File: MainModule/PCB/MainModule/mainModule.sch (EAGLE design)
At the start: 13 parts, among them U1 LM5007MM

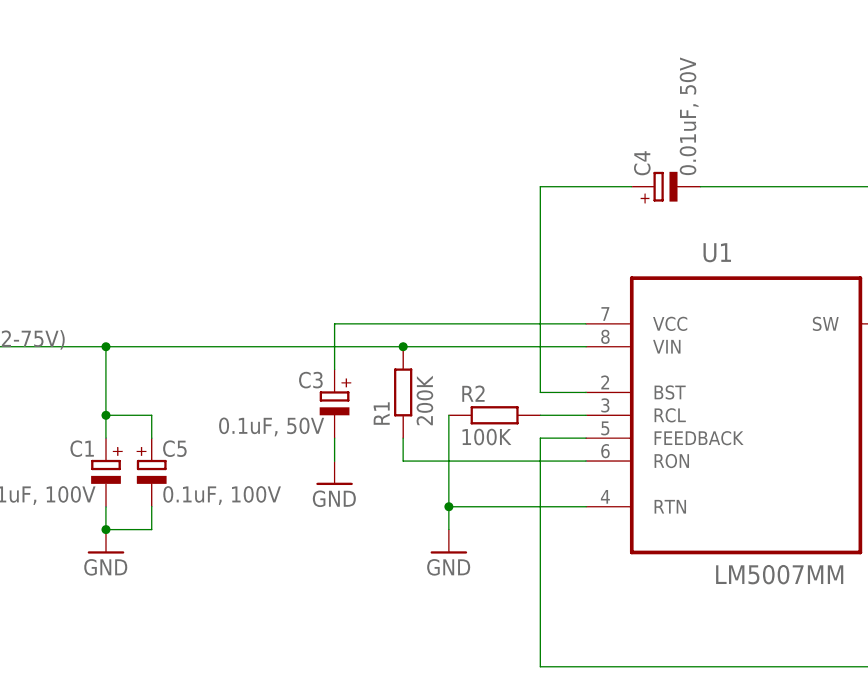
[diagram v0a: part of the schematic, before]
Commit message: Changed capacitor packages in to power supply schematic (switching)
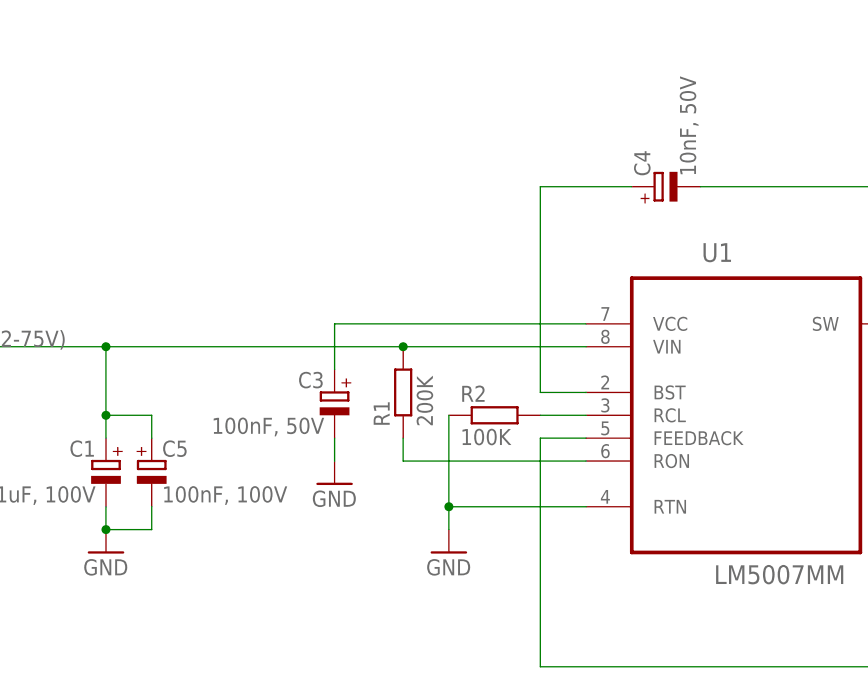
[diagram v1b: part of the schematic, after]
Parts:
- C1: device resistor:CPOL-EU140CLH-0810 -> resistor:CPOL-EU153CLV-0405
- C2: device resistor:CPOL-EU140CLH-0810 -> resistor:CPOL-EUC
- C3: value 0.1uF, 50V -> 100nF, 50V; device resistor:CPOL-EU140CLH-0810 -> resistor:CPOL-EUSMCA
- C4: value 0.01uF, 50V -> 10nF, 50V; device resistor:CPOL-EU140CLH-0810 -> resistor:CPOL-EUR/2012-12W
- C5: value 0.1uF, 100V -> 100nF, 100V; device resistor:CPOL-EU140CLH-0810 -> resistor:CPOL-EUSMCA
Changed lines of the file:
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@@
 <grid distance="0.1" unitdist="inch" unit="inch" style="lines" multiple="1" display="no" altdistance="0.01" altunitdist="inch" altunit="inch"/>
 <layers>
-<layer number="1" name="Top" color="4" fill="1" visible="no" active="no"/>
-<layer number="2" name="Route2" color="1" fill="3" visible="no" active="no"/>
-<layer number="3" name="Route3" color="4" fill="3" visible="no" active="no"/>
-<layer number="4" name="Route4" color="1" fill="4" visible="no" active="no"/>
-<layer number="5" name="Route5" color="4" fill="4" visible="no" active="no"/>
-<layer number="6" name="Route6" color="1" fill="8" visible="no" active="no"/>
-<layer number="7" name="Route7" color="4" fill="8" visible="no" active="no"/>
-<layer number="8" name="Route8" color="1" fill="2" visible="no" active="no"/>
-<layer number="9" name="Route9" color="4" fill="2" visible="no" active="no"/>
-<layer number="10" name="Route10" color="1" fill="7" visible="no" active="no"/>
-<layer number="11" name="Route11" color="4" fill="7" visible="no" active="no"/>
-<layer number="12" name="Route12" color="1" fill="5" visible="no" active="no"/>
-<layer number="13" name="Route13" color="4" fill="5" visible="no" active="no"/>
-<layer number="14" name="Route14" color="1" fill="6" visible="no" active="no"/>
-<layer number="15" name="Route15" color="4" fill="6" visible="no" active="no"/>
-<layer number="16" name="Bottom" color="1" fill="1" visible="no" active="no"/>
-<layer number="17" name="Pads" color="2" fill="1" visible="no" active="no"/>
-<layer number="18" name="Vias" color="2" fill="1" visible="no" active="no"/>
-<layer number="19" name="Unrouted" color="6" fill="1" visible="no" active="no"/>
-<layer number="20" name="Dimension" color="15" fill="1" visible="no" active="no"/>
-<layer number="21" name="tPlace" color="7" fill="1" visible="no" active="no"/>
-<layer number="22" name="bPlace" color="7" fill="1" visible="no" active="no"/>
-<layer number="23" name="tOrigins" color="15" fill="1" visible="no" active="no"/>
-<layer number="24" name="bOrigins" color="15" fill="1" visible="no" active="no"/>
-<layer number="25" name="tNames" color="7" fill="1" visible="no" active="no"/>
-<layer number="26" name="bNames" color="7" fill="1" visible="no" active="no"/>
-<layer number="27" name="tValues" color="7" fill="1" visible="no" active="no"/>
-<layer number="28" name="bValues" color="7" fill="1" visible="no" active="no"/>
+<layer number="1" name="Top" color="4" fill="1" visible="yes" active="no"/>
+<layer number="2" name="Route2" color="1" fill="3" visible="yes" active="no"/>
+<layer number="3" name="Route3" color="4" fill="3" visible="yes" active="no"/>
+<layer number="4" name="Route4" color="1" fill="4" visible="yes" active="no"/>
+<layer number="5" name="Route5" color="4" fill="4" visible="yes" active="no"/>
+<layer number="6" name="Route6" color="1" fill="8" visible="yes" active="no"/>
+<layer number="7" name="Route7" color="4" fill="8" visible="yes" active="no"/>
+<layer number="8" name="Route8" color="1" fill="2" visible="yes" active="no"/>
+<layer number="9" name="Route9" color="4" fill="2" visible="yes" active="no"/>
+<layer number="10" name="Route10" color="1" fill="7" visible="yes" active="no"/>
+<layer number="11" name="Route11" color="4" fill="7" visible="yes" active="no"/>
+<layer number="12" name="Route12" color="1" fill="5" visible="yes" active="no"/>
+<layer number="13" name="Route13" color="4" fill="5" visible="yes" active="no"/>
+<layer number="14" name="Route14" color="1" fill="6" visible="yes" active="no"/>
+<layer number="15" name="Route15" color="4" fill="6" visible="yes" active="no"/>
+<layer number="16" name="Bottom" color="1" fill="1" visible="yes" active="no"/>
+<layer number="17" name="Pads" color="2" fill="1" visible="yes" active="no"/>
+<layer number="18" name="Vias" color="2" fill="1" visible="yes" active="no"/>
+<layer number="19" name="Unrouted" color="6" fill="1" visible="yes" active="no"/>
+<layer number="20" name="Dimension" color="15" fill="1" visible="yes" active="no"/>
+<layer number="21" name="tPlace" color="7" fill="1" visible="yes" active="no"/>
+<layer number="22" name="bPlace" color="7" fill="1" visible="yes" active="no"/>
+<layer number="23" name="tOrigins" color="15" fill="1" visible="yes" active="no"/>
+<layer number="24" name="bOrigins" color="15" fill="1" visible="yes" active="no"/>
+<layer number="25" name="tNames" color="7" fill="1" visible="yes" active="no"/>
+<layer number="26" name="bNames" color="7" fill="1" visible="yes" active="no"/>
+<layer number="27" name="tValues" color="7" fill="1" visible="yes" active="no"/>
+<layer number="28" name="bValues" color="7" fill="1" visible="yes" active="no"/>
 <layer number="29" name="tStop" color="7" fill="3" visible="no" active="no"/>
 <layer number="30" name="bStop" color="7" fill="6" visible="no" active="no"/>
@@
 <layer number="35" name="tGlue" color="7" fill="4" visible="no" active="no"/>
 <layer number="36" name="bGlue" color="7" fill="5" visible="no" active="no"/>
-<layer number="37" name="tTest" color="7" fill="1" visible="no" active="no"/>
-<layer number="38" name="bTest" color="7" fill="1" visible="no" active="no"/>
+<layer number="37" name="tTest" color="7" fill="1" visible="yes" active="no"/>
+<layer number="38" name="bTest" color="7" fill="1" visible="yes" active="no"/>
 <layer number="39" name="tKeepout" color="4" fill="11" visible="no" active="no"/>
 <layer number="40" name="bKeepout" color="1" fill="11" visible="no" active="no"/>
@@
 <layer number="44" name="Drills" color="7" fill="1" visible="no" active="no"/>
 <layer number="45" name="Holes" color="7" fill="1" visible="no" active="no"/>
-<layer number="46" name="Milling" color="3" fill="1" visible="no" active="no"/>
-<layer number="47" name="Measures" color="7" fill="1" visible="no" active="no"/>
-<layer number="48" name="Document" color="7" fill="1" visible="no" active="no"/>
-<layer number="49" name="Reference" color="7" fill="1" visible="no" active="no"/>
-<layer number="51" name="tDocu" color="7" fill="1" visible="no" active="no"/>
-<layer number="52" name="bDocu" color="7" fill="1" visible="no" active="no"/>
+<layer number="46" name="Milling" color="3" fill="1" visible="yes" active="no"/>
+<layer number="47" name="Measures" color="7" fill="1" visible="yes" active="no"/>
+<layer number="48" name="Document" color="7" fill="1" visible="yes" active="no"/>
+<layer number="49" name="Reference" color="7" fill="1" visible="yes" active="no"/>
+<layer number="51" name="tDocu" color="7" fill="1" visible="yes" active="no"/>
+<layer number="52" name="bDocu" color="7" fill="1" visible="yes" active="no"/>
 <layer number="91" name="Nets" color="2" fill="1" visible="yes" active="yes"/>
 <layer number="92" name="Busses" color="1" fill="1" visible="yes" active="yes"/>
@@
 <part name="U1" library="LM5007" deviceset="LM5007MM" device=""/>
 <part name="FRAME1" library="frames" deviceset="A4L-LOC" device=""/>
-<part name="C1" library="resistor" deviceset="CPOL-EU" device="140CLH-0810" value="1uF, 100V"/>
-<part name="C2" library="resistor" deviceset="CPOL-EU" device="140CLH-0810" value="15uF, 25V"/>
-<part name="C3" library="resistor" deviceset="CPOL-EU" device="140CLH-0810" value="0.1uF, 50V"/>
-<part name="C4" library="resistor" deviceset="CPOL-EU" device="140CLH-0810" value="0.01uF, 50V"/>
-<part name="C5" library="resistor" deviceset="CPOL-EU" device="140CLH-0810" value="0.1uF, 100V"/>
+<part name="C1" library="resistor" deviceset="CPOL-EU" device="153CLV-0405" value="1uF, 100V"/>
+<part name="C2" library="resistor" deviceset="CPOL-EU" device="C" value="15uF, 25V"/>
+<part name="C3" library="resistor" deviceset="CPOL-EU" device="SMCA" value="100nF, 50V"/>
+<part name="C4" library="resistor" deviceset="CPOL-EU" device="R/2012-12W" value="10nF, 50V"/>
+<part name="C5" library="resistor" deviceset="CPOL-EU" device="SMCA" value="100nF, 100V"/>
 <part name="L1" library="inductor-neosid" deviceset="SM-Z15" device="" value="100uH"/>
 <part name="R1" library="rcl" deviceset="R-EU_" device="R2010" value="200K"/>

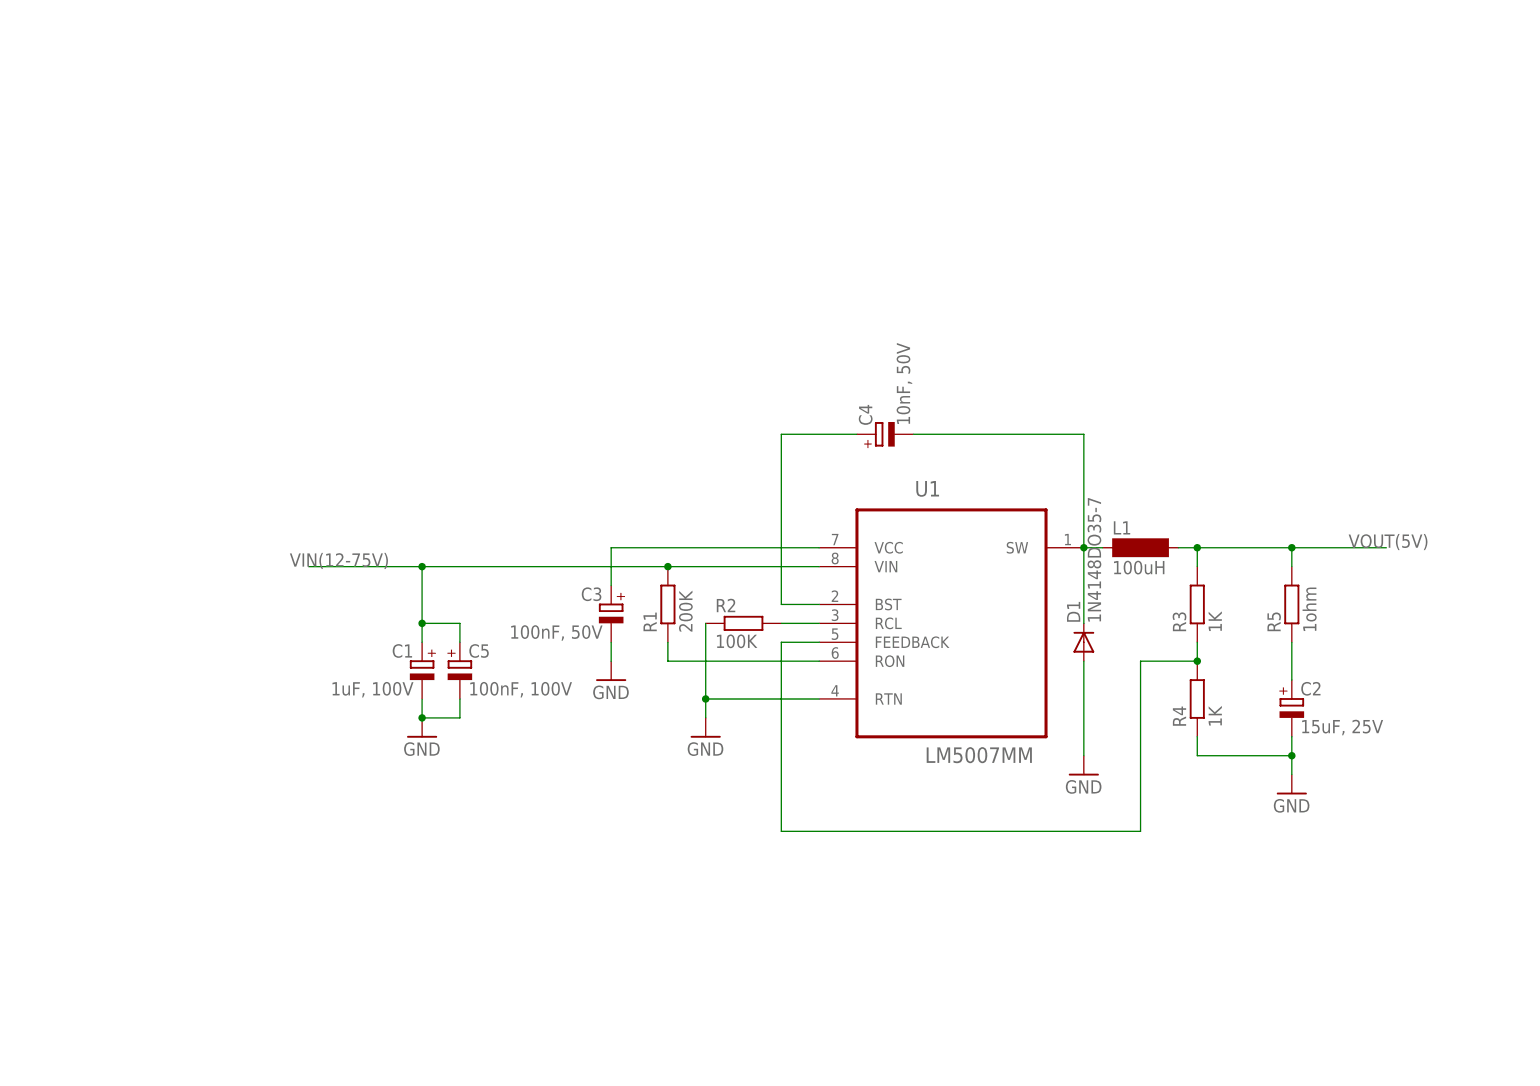
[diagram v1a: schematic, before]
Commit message: Added linear regulator LM3940.lbr library
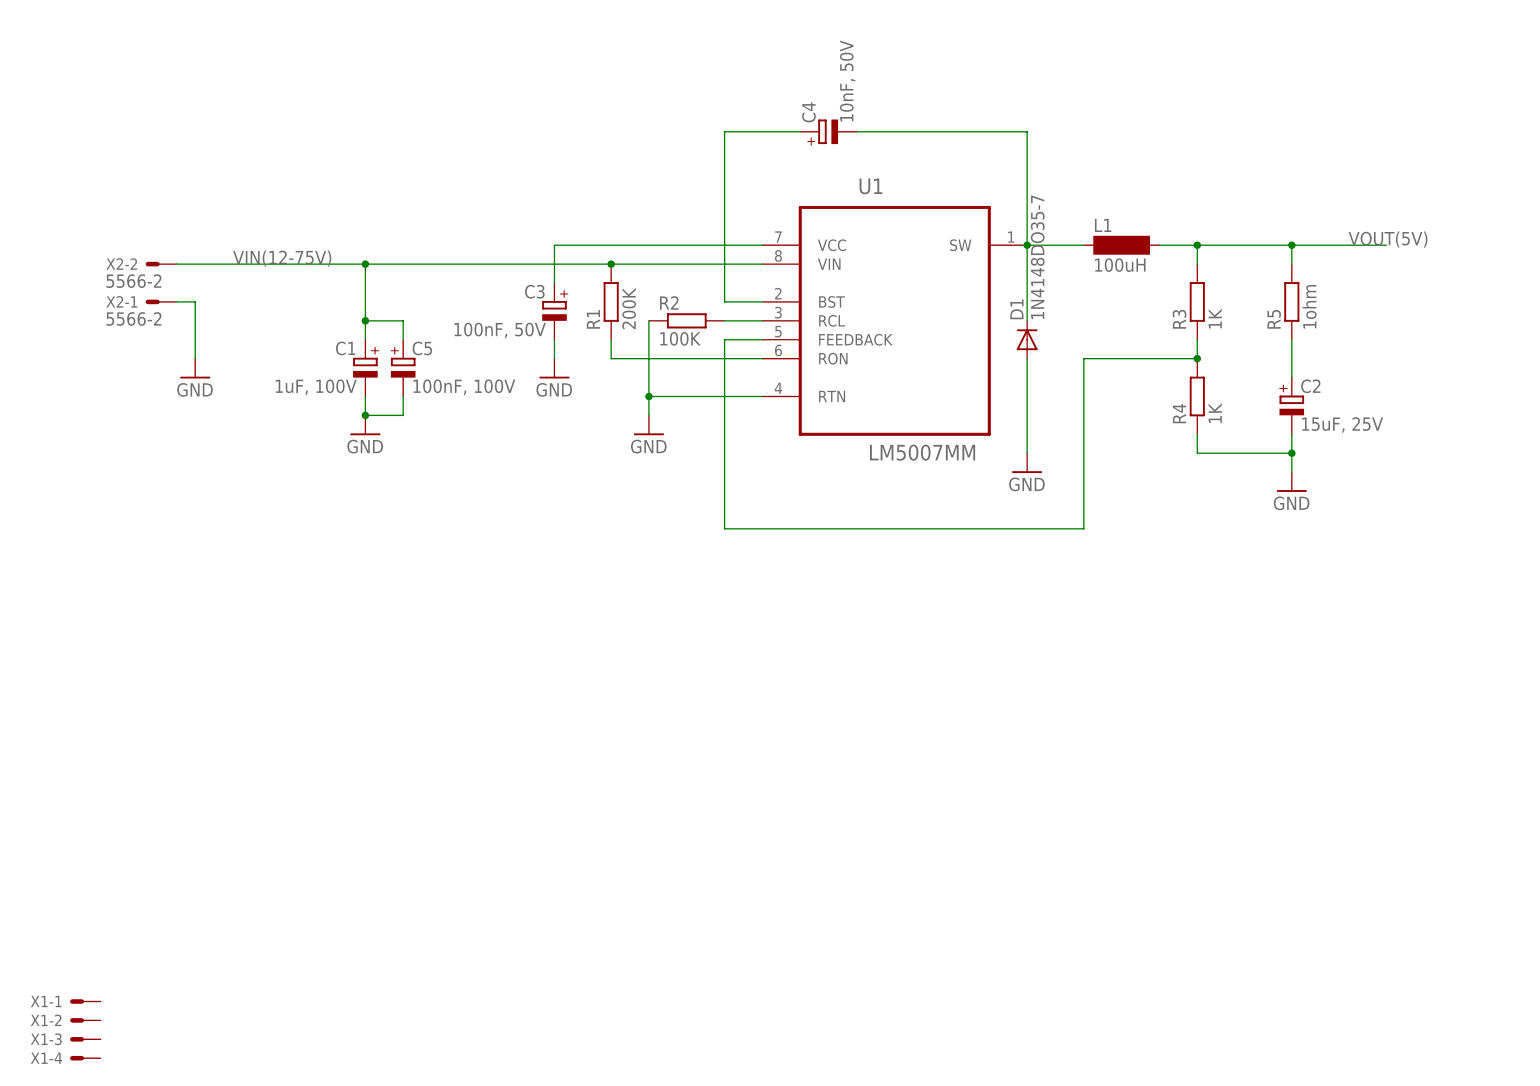
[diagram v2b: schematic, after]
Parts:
- added X1: (no value), con-molex:KK-156-4
- added X2: 5566-2, con-molex:5566-2
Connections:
- net GND: now also X2-1.S
- net VIN(12-75V): now also X2-2.S
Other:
- moved on the sheet: C1, C2, C3, C4, C5, D1, L1, R1, R2, R3, R4, R5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

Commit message: Wiring circuit for liner regulator (LM3940)
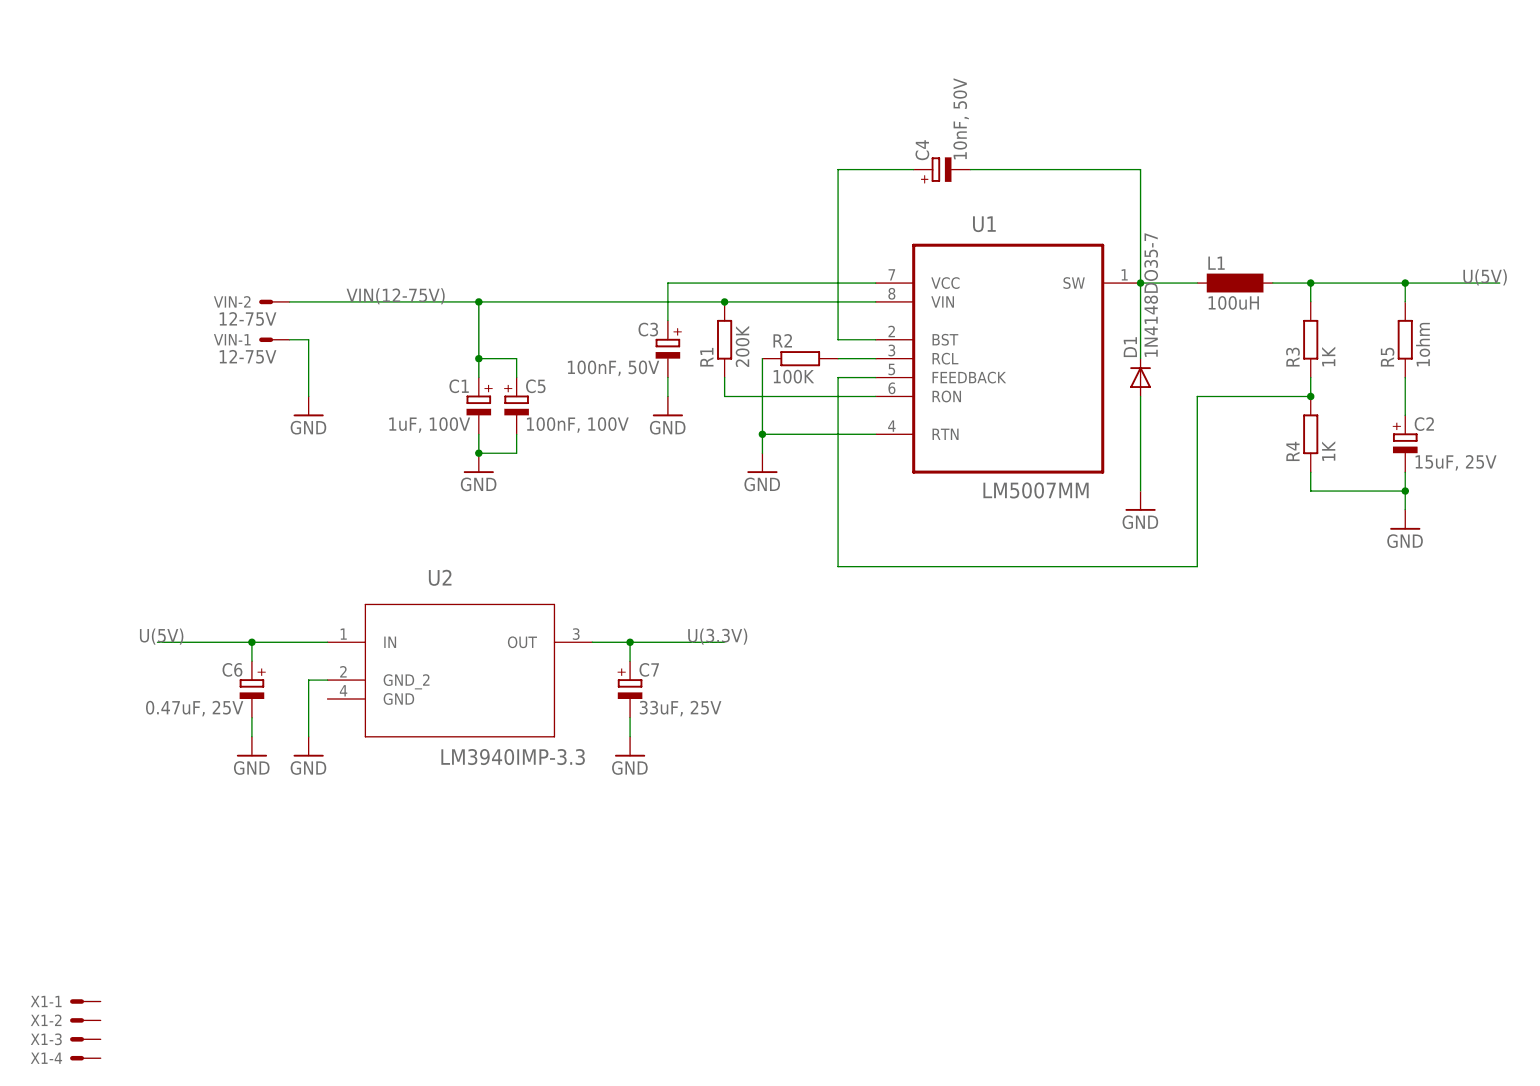
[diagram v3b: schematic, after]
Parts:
- removed X2: 5566-2, con-molex:5566-2
- added C6: 0.47uF, 25V, resistor:CPOL-EUC
- added C7: 33uF, 25V, resistor:CPOL-EUC
- added U2: LM3940IMP-3.3, LM3940:LM3940IMP-3.3
- added VIN: 12-75V, con-molex:5566-2
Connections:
- removed net VOUT(5V): L1.2, R3.2, R5.2
- new net U(3.3V): C7.+, U2.OUT
- new net U(5V): C6.+, L1.2, R3.2, R5.2, U2.IN
- net GND: now also C6.-, C7.-, U2.GND_2, VIN-1.S; no longer X2-1.S
- net VIN(12-75V): now also VIN-2.S; no longer X2-2.S
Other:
- moved on the sheet: C1, C2, C3, C4, C5, D1, L1, R1, R2, R3, R4, R5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

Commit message: Added LPCXpresso boards library
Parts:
- added LPC1: (no value), LPCXpresso_LPC1769_board:LPCXPRESSO_LPC1769
- added X2: MINI-USB-32005-201, con-cypressindustries:MINI-USB-32005-201
